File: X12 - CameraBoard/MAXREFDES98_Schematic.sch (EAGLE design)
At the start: 26 parts, among them U1 MB110S-TP, U2 MB110S-TP, U3 MAX5969AETB+, U4 MAX17503ATP+

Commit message: Fixing 0-Ohm Resistor stuff
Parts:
- removed J1: (no value), SparkFun-Connectors:CONN_01
- removed R7: 0, SparkFun-Resistors:0OHM-0603-1/10W-5%
- added R10, R11, R8, R9: 0, SparkFun-Resistors:0OHM-0603-1/10W-5%
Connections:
- removed net IND_2_OUT: C10.1, C4.1, L2.2, R4.2, R7.1
- net 5V_OUT: now also C10.1, C4.1, L2.2, R11.1, R4.2, R8.1; no longer J1.1, R7.2
- net GND: now also R10.1, R9.1
- net RECT1_IN_MINUS: now also R10.2
- net RECT1_IN_PLUS: now also R8.2
- net RECT2_IN_MINUS: now also R9.2
- net RECT2_IN_PLUS: now also R11.2
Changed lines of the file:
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@@
 <part name="CONN" library="Camera_Board_Parts_09_30_2020" deviceset="TERM_BLOCK_PLUG_8POS_STR_2.5MM" device=""/>
 <part name="U$2" library="Camera_Board_Parts_09_30_2020" deviceset="NANO_PI" device=""/>
-<part name="R7" library="SparkFun-Resistors" library_urn="urn:adsk.eagle:library:532" deviceset="0OHM" device="-0603-1/10W-5%" package3d_urn="urn:adsk.eagle:package:39650/1" value="0"/>
-<part name="J1" library="SparkFun-Connectors" library_urn="urn:adsk.eagle:library:513" deviceset="CONN_01" device="" package3d_urn="urn:adsk.eagle:package:38028/1"/>
+<part name="R10" library="SparkFun-Resistors" library_urn="urn:adsk.eagle:library:532" deviceset="0OHM" device="-0603-1/10W-5%" package3d_urn="urn:adsk.eagle:package:39650/1" value="0"/>
+<part name="R8" library="SparkFun-Resistors" library_urn="urn:adsk.eagle:library:532" deviceset="0OHM" device="-0603-1/10W-5%" package3d_urn="urn:adsk.eagle:package:39650/1" value="0"/>
+<part name="R9" library="SparkFun-Resistors" library_urn="urn:adsk.eagle:library:532" deviceset="0OHM" device="-0603-1/10W-5%" package3d_urn="urn:adsk.eagle:package:39650/1" value="0"/>
+<part name="R11" library="SparkFun-Resistors" library_urn="urn:adsk.eagle:library:532" deviceset="0OHM" device="-0603-1/10W-5%" package3d_urn="urn:adsk.eagle:package:39650/1" value="0"/>
+<part name="GND9" library="supply1" library_urn="urn:adsk.eagle:library:371" deviceset="GND" device=""/>
+<part name="GND14" library="supply1" library_urn="urn:adsk.eagle:library:371" deviceset="GND" device=""/>
 </parts>
 <sheets>
@@
 </instance>
 <instance part="U$2" gate="G$1" x="20.32" y="-119.38" smashed="yes"/>
-<instance part="R7" gate="G$1" x="271.78" y="0" smashed="yes">
-<attribute name="NAME" x="271.78" y="1.524" size="1.778" layer="95" font="vector" align="bottom-center"/>
-<attribute name="VALUE" x="271.78" y="-1.524" size="1.778" layer="96" font="vector" align="top-center"/>
-</instance>
-<instance part="J1" gate="G$1" x="276.86" y="-12.7" smashed="yes" rot="R90">
-<attribute name="VALUE" x="281.686" y="-15.24" size="1.778" layer="96" font="vector" rot="R90"/>
-<attribute name="NAME" x="273.812" y="-15.24" size="1.778" layer="95" font="vector" rot="R90"/>
+<instance part="R10" gate="G$1" x="-114.3" y="-22.86" smashed="yes" rot="R90">
+<attribute name="NAME" x="-115.824" y="-22.86" size="1.778" layer="95" font="vector" rot="R90" align="bottom-center"/>
+<attribute name="VALUE" x="-112.776" y="-22.86" size="1.778" layer="96" font="vector" rot="R90" align="top-center"/>
+</instance>
+<instance part="R8" gate="G$1" x="-109.22" y="-22.86" smashed="yes" rot="R90">
+<attribute name="NAME" x="-110.744" y="-22.86" size="1.778" layer="95" font="vector" rot="R90" align="bottom-center"/>
+<attribute name="VALUE" x="-107.696" y="-22.86" size="1.778" layer="96" font="vector" rot="R90" align="top-center"/>
+</instance>
+<instance part="R9" gate="G$1" x="-99.06" y="-22.86" smashed="yes" rot="R90">
+<attribute name="NAME" x="-100.584" y="-22.86" size="1.778" layer="95" font="vector" rot="R90" align="bottom-center"/>
+<attribute name="VALUE" x="-97.536" y="-22.86" size="1.778" layer="96" font="vector" rot="R90" align="top-center"/>
+</instance>
+<instance part="R11" gate="G$1" x="-93.98" y="-22.86" smashed="yes" rot="R90">
+<attribute name="NAME" x="-95.504" y="-22.86" size="1.778" layer="95" font="vector" rot="R90" align="bottom-center"/>
+<attribute name="VALUE" x="-92.456" y="-22.86" size="1.778" layer="96" font="vector" rot="R90" align="top-center"/>
+</instance>
+<instance part="GND9" gate="1" x="-114.3" y="-30.48" smashed="yes">
+<attribute name="VALUE" x="-116.84" y="-33.02" size="1.778" layer="96"/>
+</instance>
+<instance part="GND14" gate="1" x="-99.06" y="-30.48" smashed="yes">
+<attribute name="VALUE" x="-101.6" y="-33.02" size="1.778" layer="96"/>
 </instance>
 </instances>
@@
 </segment>
 <segment>
-<pinref part="R7" gate="G$1" pin="2"/>
-<pinref part="J1" gate="G$1" pin="1"/>
-<wire x1="276.86" y1="0" x2="276.86" y2="-5.08" width="0.1524" layer="91"/>
-<wire x1="276.86" y1="0" x2="281.94" y2="0" width="0.1524" layer="91"/>
-<junction x="276.86" y="0"/>
-<label x="276.86" y="0" size="1.778" layer="95"/>
+<pinref part="R8" gate="G$1" pin="1"/>
+<wire x1="-109.22" y1="-27.94" x2="-109.22" y2="-35.56" width="0.1524" layer="91"/>
+<label x="-109.22" y="-38.1" size="1.778" layer="95"/>
+</segment>
+<segment>
+<pinref part="R11" gate="G$1" pin="1"/>
+<wire x1="-93.98" y1="-27.94" x2="-93.98" y2="-35.56" width="0.1524" layer="91"/>
+<label x="-93.98" y="-38.1" size="1.778" layer="95"/>
+</segment>
+<segment>
+<pinref part="C4" gate="G$1" pin="1"/>
+<pinref part="C10" gate="G$1" pin="1"/>
+<wire x1="226.06" y1="0" x2="238.76" y2="0" width="0.1524" layer="91"/>
+<junction x="226.06" y="0"/>
+<pinref part="L2" gate="G$1" pin="2"/>
+<wire x1="223.52" y1="0" x2="226.06" y2="0" width="0.1524" layer="91"/>
+<pinref part="R4" gate="G$1" pin="2"/>
+<wire x1="238.76" y1="0" x2="254" y2="0" width="0.1524" layer="91"/>
+<wire x1="254" y1="0" x2="254" y2="-7.62" width="0.1524" layer="91"/>
+<junction x="238.76" y="0"/>
+<wire x1="254" y1="0" x2="266.7" y2="0" width="0.1524" layer="91"/>
+<junction x="254" y="0"/>
+<label x="266.7" y="2.54" size="1.778" layer="95" rot="R180"/>
 </segment>
 </net>
@@
 <label x="5.08" y="-83.82" size="1.778" layer="95"/>
 </segment>
+<segment>
+<pinref part="GND9" gate="1" pin="GND"/>
+<pinref part="R10" gate="G$1" pin="1"/>
+</segment>
+<segment>
+<pinref part="GND14" gate="1" pin="GND"/>
+<pinref part="R9" gate="G$1" pin="1"/>
+</segment>
 </net>
 <net name="RESET" class="0">
@@
 <net name="RECT1_IN_MINUS" class="0">
 <segment>
-<wire x1="-114.3" y1="-12.7" x2="-114.3" y2="-7.62" width="0.1524" layer="91"/>
-<pinref part="U1" gate="G$1" pin="~1"/>
-<label x="-114.3" y="-33.02" size="1.778" layer="95" rot="R90"/>
-</segment>
-<segment>
 <pinref part="CONN" gate="G$1" pin="2"/>
 <wire x1="-71.12" y1="-73.66" x2="-71.12" y2="-68.58" width="0.1524" layer="91"/>
 <label x="-71.12" y="-68.58" size="1.778" layer="95" rot="R90"/>
 </segment>
+<segment>
+<pinref part="U1" gate="G$1" pin="~1"/>
+<pinref part="R10" gate="G$1" pin="2"/>
+<wire x1="-114.3" y1="-7.62" x2="-114.3" y2="-17.78" width="0.1524" layer="91"/>
+<label x="-116.84" y="-20.32" size="1.778" layer="95" rot="R90"/>
+</segment>
 </net>
 <net name="RECT1_IN_PLUS" class="0">
-<segment>
-<wire x1="-109.22" y1="-12.7" x2="-109.22" y2="-7.62" width="0.1524" layer="91"/>
-<pinref part="U1" gate="G$1" pin="~2"/>
-<label x="-109.22" y="-33.02" size="1.778" layer="95" rot="R90"/>
-</segment>
 <segment>
 <pinref part="CONN" gate="G$1" pin="1"/>
@@
 <label x="-73.66" y="-68.58" size="1.778" layer="95" rot="R90"/>
 </segment>
+<segment>
+<pinref part="U1" gate="G$1" pin="~2"/>
+<pinref part="R8" gate="G$1" pin="2"/>
+<wire x1="-109.22" y1="-7.62" x2="-109.22" y2="-17.78" width="0.1524" layer="91"/>
+<label x="-106.68" y="-20.32" size="1.778" layer="95" rot="R90"/>
+</segment>
 </net>
 <net name="RECT2_IN_MINUS" class="0">
-<segment>
-<wire x1="-99.06" y1="-12.7" x2="-99.06" y2="-7.62" width="0.1524" layer="91"/>
-<pinref part="U2" gate="G$1" pin="~1"/>
-<label x="-99.06" y="-33.02" size="1.778" layer="95" rot="R90"/>
-</segment>
 <segment>
 <pinref part="CONN" gate="G$1" pin="3"/>
@@
 <label x="-68.58" y="-68.58" size="1.778" layer="95" rot="R90"/>
 </segment>
+<segment>
+<pinref part="U2" gate="G$1" pin="~1"/>
+<pinref part="R9" gate="G$1" pin="2"/>
+<wire x1="-99.06" y1="-7.62" x2="-99.06" y2="-17.78" width="0.1524" layer="91"/>
+<label x="-99.06" y="-20.32" size="1.778" layer="95" rot="R90"/>
+</segment>
 </net>
 <net name="RECT2_IN_PLUS" class="0">
-<segment>
-<wire x1="-93.98" y1="-12.7" x2="-93.98" y2="-7.62" width="0.1524" layer="91"/>
-<pinref part="U2" gate="G$1" pin="~2"/>
-<label x="-93.98" y="-33.02" size="1.778" layer="95" rot="R90"/>
-</segment>
 <segment>
 <pinref part="CONN" gate="G$1" pin="4"/>
@@
 <label x="-66.04" y="-68.58" size="1.778" layer="95" rot="R90"/>
 </segment>
+<segment>
+<pinref part="U2" gate="G$1" pin="~2"/>
+<pinref part="R11" gate="G$1" pin="2"/>
+<wire x1="-93.98" y1="-7.62" x2="-93.98" y2="-17.78" width="0.1524" layer="91"/>
+<label x="-91.44" y="-20.32" size="1.778" layer="95" rot="R90"/>
+</segment>
 </net>
 <net name="RD-" class="0">
@@
 </segment>
 </net>
-<net name="IND_2_OUT" class="0">
-<segment>
-<pinref part="C4" gate="G$1" pin="1"/>
-<pinref part="C10" gate="G$1" pin="1"/>
-<wire x1="226.06" y1="0" x2="238.76" y2="0" width="0.1524" layer="91"/>
-<junction x="226.06" y="0"/>
-<pinref part="L2" gate="G$1" pin="2"/>
-<wire x1="223.52" y1="0" x2="226.06" y2="0" width="0.1524" layer="91"/>
-<pinref part="R4" gate="G$1" pin="2"/>
-<wire x1="238.76" y1="0" x2="254" y2="0" width="0.1524" layer="91"/>
-<wire x1="254" y1="0" x2="254" y2="-7.62" width="0.1524" layer="91"/>
-<junction x="238.76" y="0"/>
-<wire x1="254" y1="0" x2="266.7" y2="0" width="0.1524" layer="91"/>
-<junction x="254" y="0"/>
-<label x="266.7" y="2.54" size="1.778" layer="95" rot="R180"/>
-<pinref part="R7" gate="G$1" pin="1"/>
-</segment>
-</net>

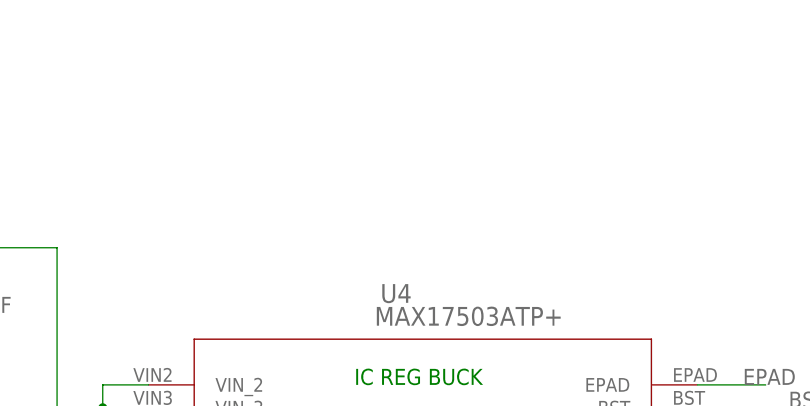
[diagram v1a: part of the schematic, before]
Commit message: Added New Buck Regultor (needs to be connected with new supporting circuitry)
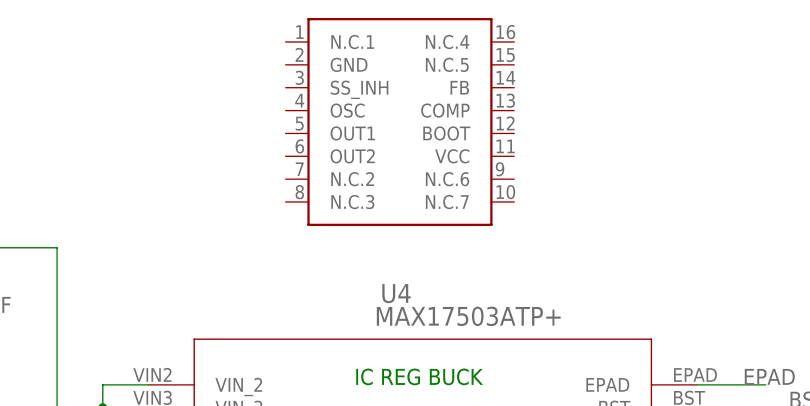
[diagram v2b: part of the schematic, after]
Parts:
- added U$1: L4978D013TR, Camera_Board_Parts_09_30_2020:L4978D013TR
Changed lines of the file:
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@@
 <part name="GND9" library="supply1" library_urn="urn:adsk.eagle:library:371" deviceset="GND" device=""/>
 <part name="GND14" library="supply1" library_urn="urn:adsk.eagle:library:371" deviceset="GND" device=""/>
+<part name="U$1" library="Camera_Board_Parts_09_30_2020" deviceset="L4978D013TR" device=""/>
 </parts>
 <sheets>
@@
 <attribute name="VALUE" x="-101.6" y="-33.02" size="1.778" layer="96"/>
 </instance>
+<instance part="U$1" gate="G$1" x="147.32" y="35.56" smashed="yes"/>
 </instances>
 <busses>

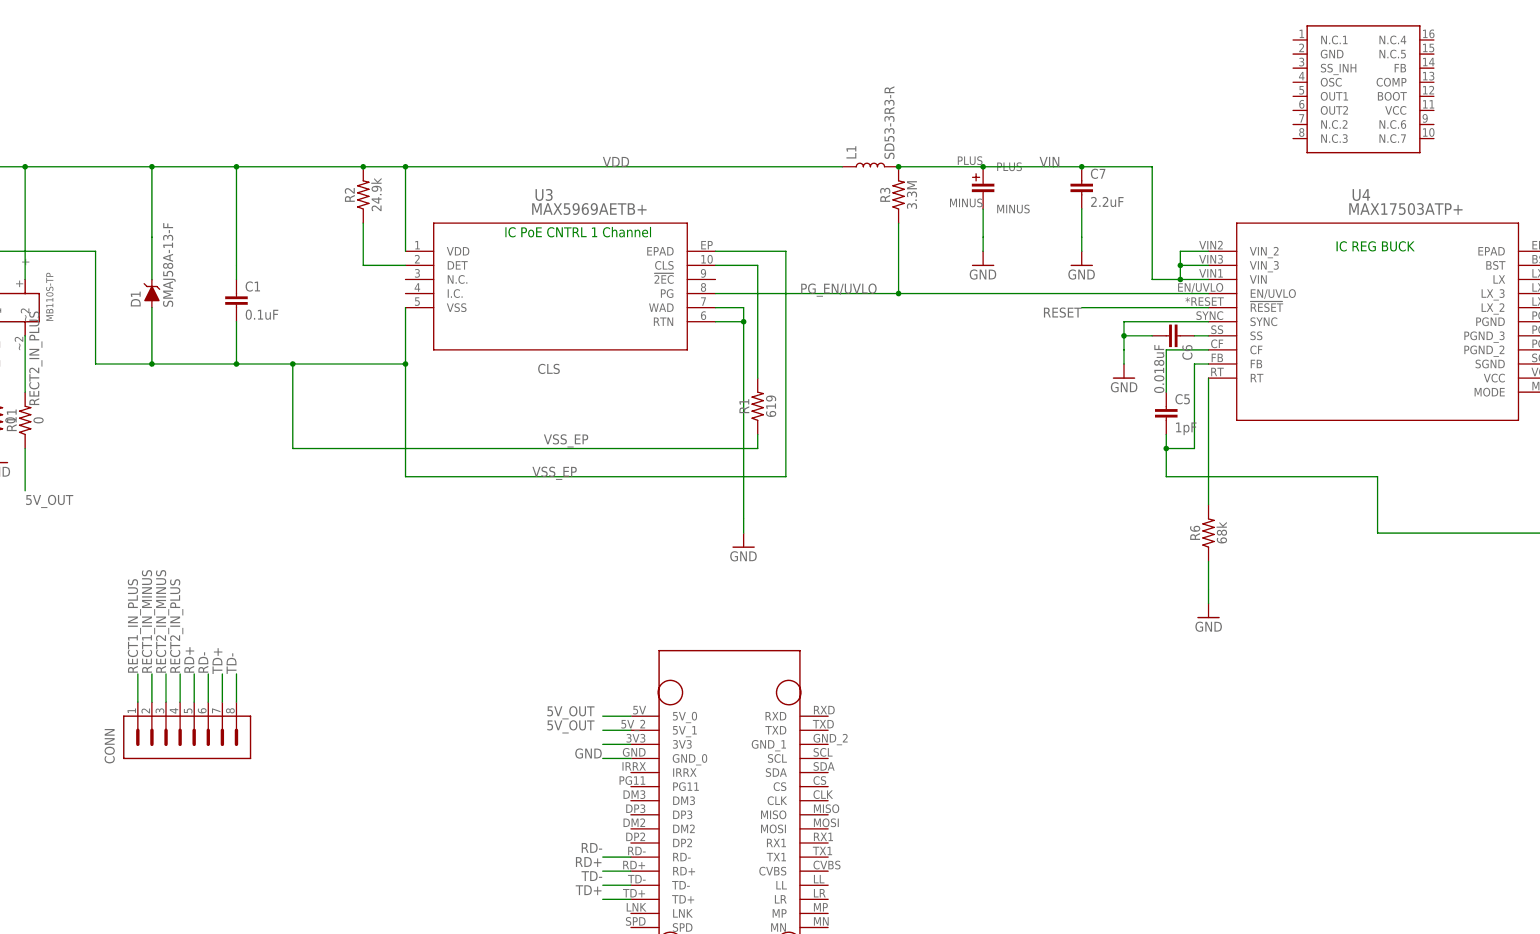
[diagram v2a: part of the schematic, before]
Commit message: Routing
Definetely need to change buck regulator because of spacing and soldering issues. Will do that soonish.
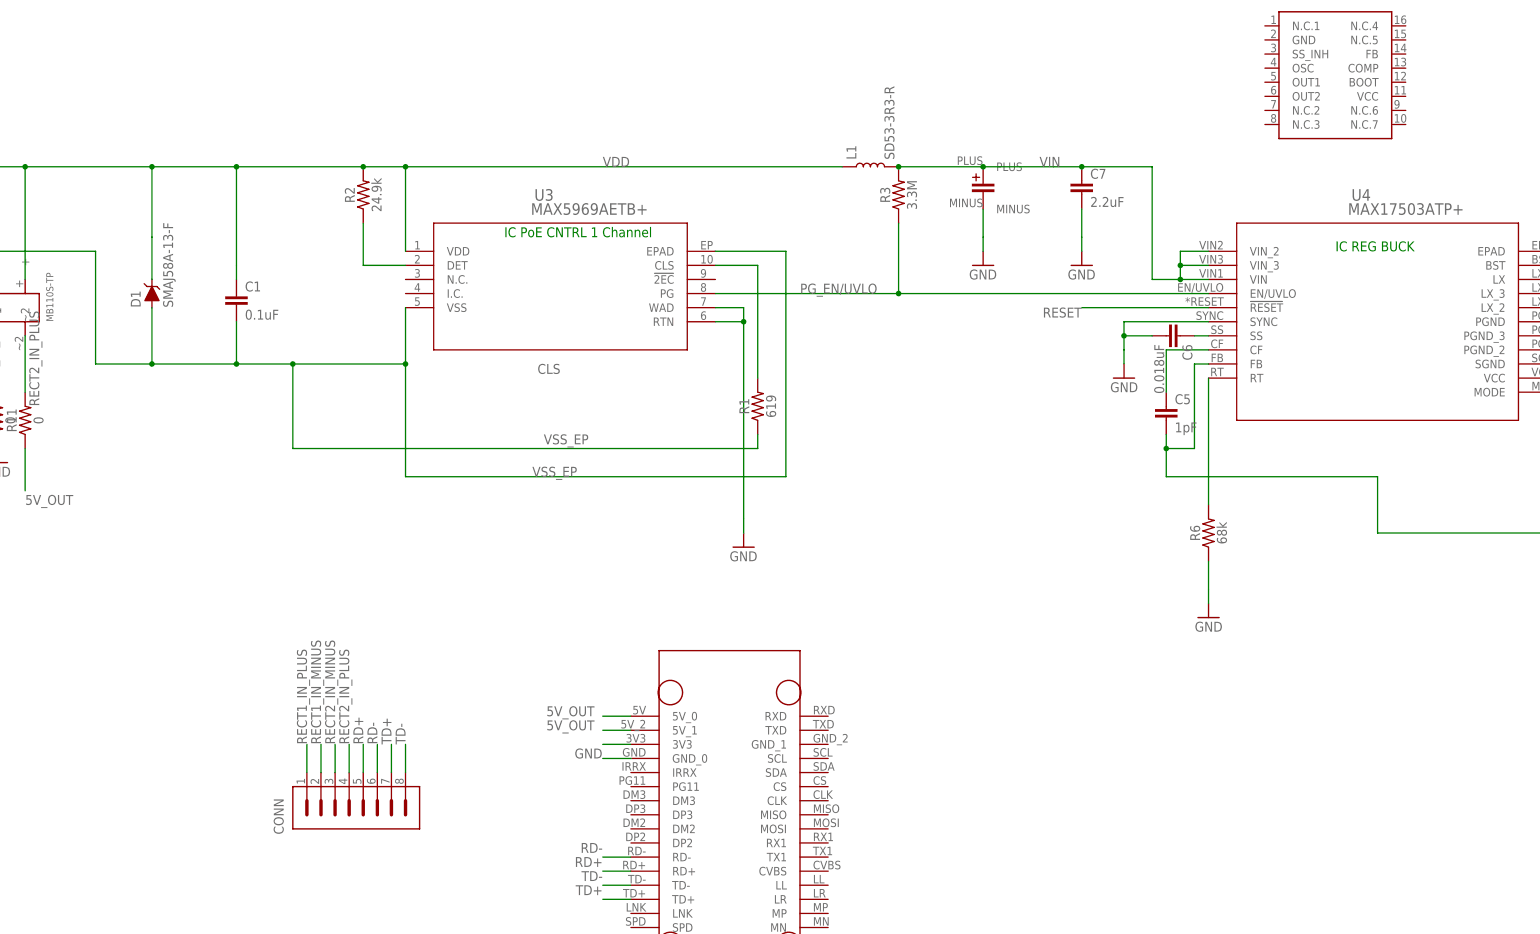
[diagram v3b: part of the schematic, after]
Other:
- moved on the sheet: CONN
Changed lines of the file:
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@@
 <attribute name="DRAWING_NAME" x="203.2" y="-125.73" size="2.54" layer="94"/>
 </instance>
-<instance part="CONN" gate="G$1" x="-76.2" y="-76.2" smashed="yes">
-<attribute name="NAME" x="-77.851" y="-84.836" size="1.778" layer="95" rot="R90"/>
+<instance part="CONN" gate="G$1" x="-45.72" y="-88.9" smashed="yes">
+<attribute name="NAME" x="-47.371" y="-97.536" size="1.778" layer="95" rot="R90"/>
 </instance>
 <instance part="U$2" gate="G$1" x="20.32" y="-119.38" smashed="yes"/>
@@
 <attribute name="VALUE" x="-101.6" y="-33.02" size="1.778" layer="96"/>
 </instance>
-<instance part="U$1" gate="G$1" x="147.32" y="35.56" smashed="yes"/>
+<instance part="U$1" gate="G$1" x="142.24" y="38.1" smashed="yes"/>
 </instances>
 <busses>
@@
 <net name="RD+" class="0">
 <segment>
-<wire x1="-63.5" y1="-73.66" x2="-63.5" y2="-68.58" width="0.1524" layer="91"/>
+<wire x1="-33.02" y1="-86.36" x2="-33.02" y2="-81.28" width="0.1524" layer="91"/>
 <pinref part="CONN" gate="G$1" pin="5"/>
-<label x="-63.5" y="-68.58" size="1.778" layer="95" rot="R90"/>
+<label x="-33.02" y="-81.28" size="1.778" layer="95" rot="R90"/>
 </segment>
 <segment>
@@
 <segment>
 <pinref part="CONN" gate="G$1" pin="2"/>
-<wire x1="-71.12" y1="-73.66" x2="-71.12" y2="-68.58" width="0.1524" layer="91"/>
-<label x="-71.12" y="-68.58" size="1.778" layer="95" rot="R90"/>
+<wire x1="-40.64" y1="-86.36" x2="-40.64" y2="-81.28" width="0.1524" layer="91"/>
+<label x="-40.64" y="-81.28" size="1.778" layer="95" rot="R90"/>
 </segment>
 <segment>
@@
 <segment>
 <pinref part="CONN" gate="G$1" pin="1"/>
-<wire x1="-73.66" y1="-73.66" x2="-73.66" y2="-68.58" width="0.1524" layer="91"/>
-<label x="-73.66" y="-68.58" size="1.778" layer="95" rot="R90"/>
+<wire x1="-43.18" y1="-86.36" x2="-43.18" y2="-81.28" width="0.1524" layer="91"/>
+<label x="-43.18" y="-81.28" size="1.778" layer="95" rot="R90"/>
 </segment>
 <segment>
@@
 <segment>
 <pinref part="CONN" gate="G$1" pin="3"/>
-<wire x1="-68.58" y1="-73.66" x2="-68.58" y2="-68.58" width="0.1524" layer="91"/>
-<label x="-68.58" y="-68.58" size="1.778" layer="95" rot="R90"/>
+<wire x1="-38.1" y1="-86.36" x2="-38.1" y2="-81.28" width="0.1524" layer="91"/>
+<label x="-38.1" y="-81.28" size="1.778" layer="95" rot="R90"/>
 </segment>
 <segment>
@@
 <segment>
 <pinref part="CONN" gate="G$1" pin="4"/>
-<wire x1="-66.04" y1="-73.66" x2="-66.04" y2="-68.58" width="0.1524" layer="91"/>
-<label x="-66.04" y="-68.58" size="1.778" layer="95" rot="R90"/>
+<wire x1="-35.56" y1="-86.36" x2="-35.56" y2="-81.28" width="0.1524" layer="91"/>
+<label x="-35.56" y="-81.28" size="1.778" layer="95" rot="R90"/>
 </segment>
 <segment>
@@
 <segment>
 <pinref part="CONN" gate="G$1" pin="6"/>
-<wire x1="-60.96" y1="-73.66" x2="-60.96" y2="-68.58" width="0.1524" layer="91"/>
-<label x="-60.96" y="-68.58" size="1.778" layer="95" rot="R90"/>
+<wire x1="-30.48" y1="-86.36" x2="-30.48" y2="-81.28" width="0.1524" layer="91"/>
+<label x="-30.48" y="-81.28" size="1.778" layer="95" rot="R90"/>
 </segment>
 <segment>
@@
 <segment>
 <pinref part="CONN" gate="G$1" pin="7"/>
-<wire x1="-58.42" y1="-73.66" x2="-58.42" y2="-68.58" width="0.1524" layer="91"/>
-<label x="-58.42" y="-68.58" size="1.778" layer="95" rot="R90"/>
+<wire x1="-27.94" y1="-86.36" x2="-27.94" y2="-81.28" width="0.1524" layer="91"/>
+<label x="-27.94" y="-81.28" size="1.778" layer="95" rot="R90"/>
 </segment>
 <segment>
@@
 <segment>
 <pinref part="CONN" gate="G$1" pin="8"/>
-<wire x1="-55.88" y1="-73.66" x2="-55.88" y2="-68.58" width="0.1524" layer="91"/>
-<label x="-55.88" y="-68.58" size="1.778" layer="95" rot="R90"/>
-</segment>
-<segment>
+<wire x1="-25.4" y1="-86.36" x2="-25.4" y2="-81.28" width="0.1524" layer="91"/>
+<label x="-25.4" y="-81.28" size="1.778" layer="95" rot="R90"/>
+</segment>
+<segment>
